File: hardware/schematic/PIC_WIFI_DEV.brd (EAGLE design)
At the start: 111.5 x 26.4 mm, 60 parts, among them J5 POWER_JACKPTH, Q1 8MHz, Q2 32.768KHz, U1 PIC32MX460F512L TQFP100, U4 RECOM_X.X_REG78XX

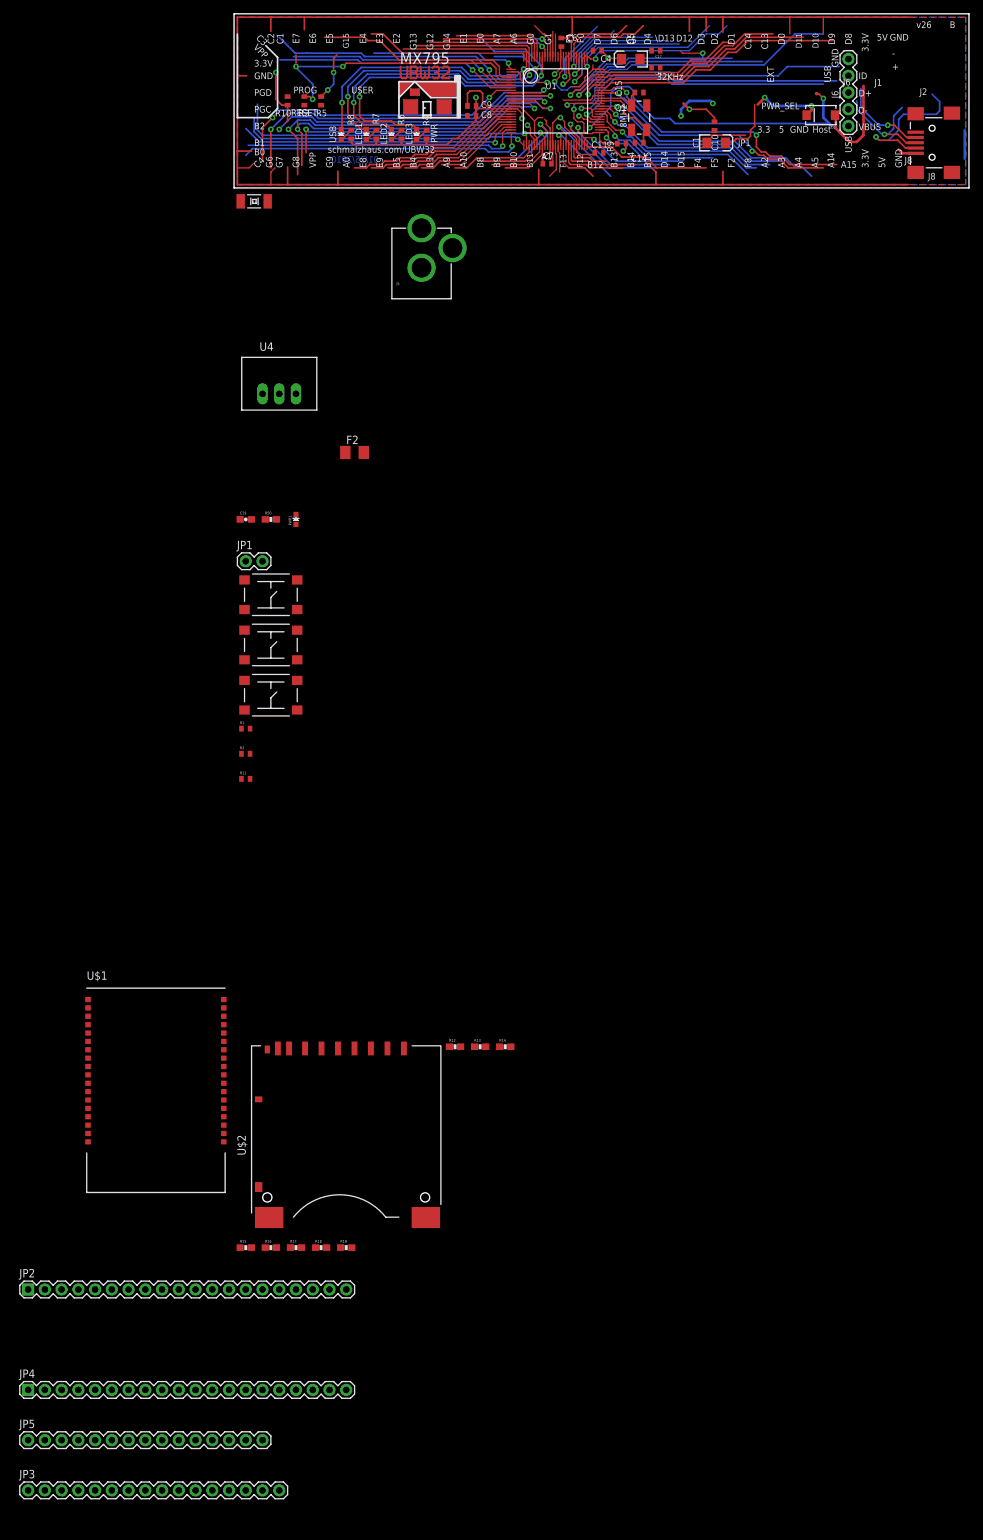
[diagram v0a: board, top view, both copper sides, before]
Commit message: Added fuse holder to lib.  Swapped 10k res for 2 4.7K in dev board.  Added fuse to waterworx.sch
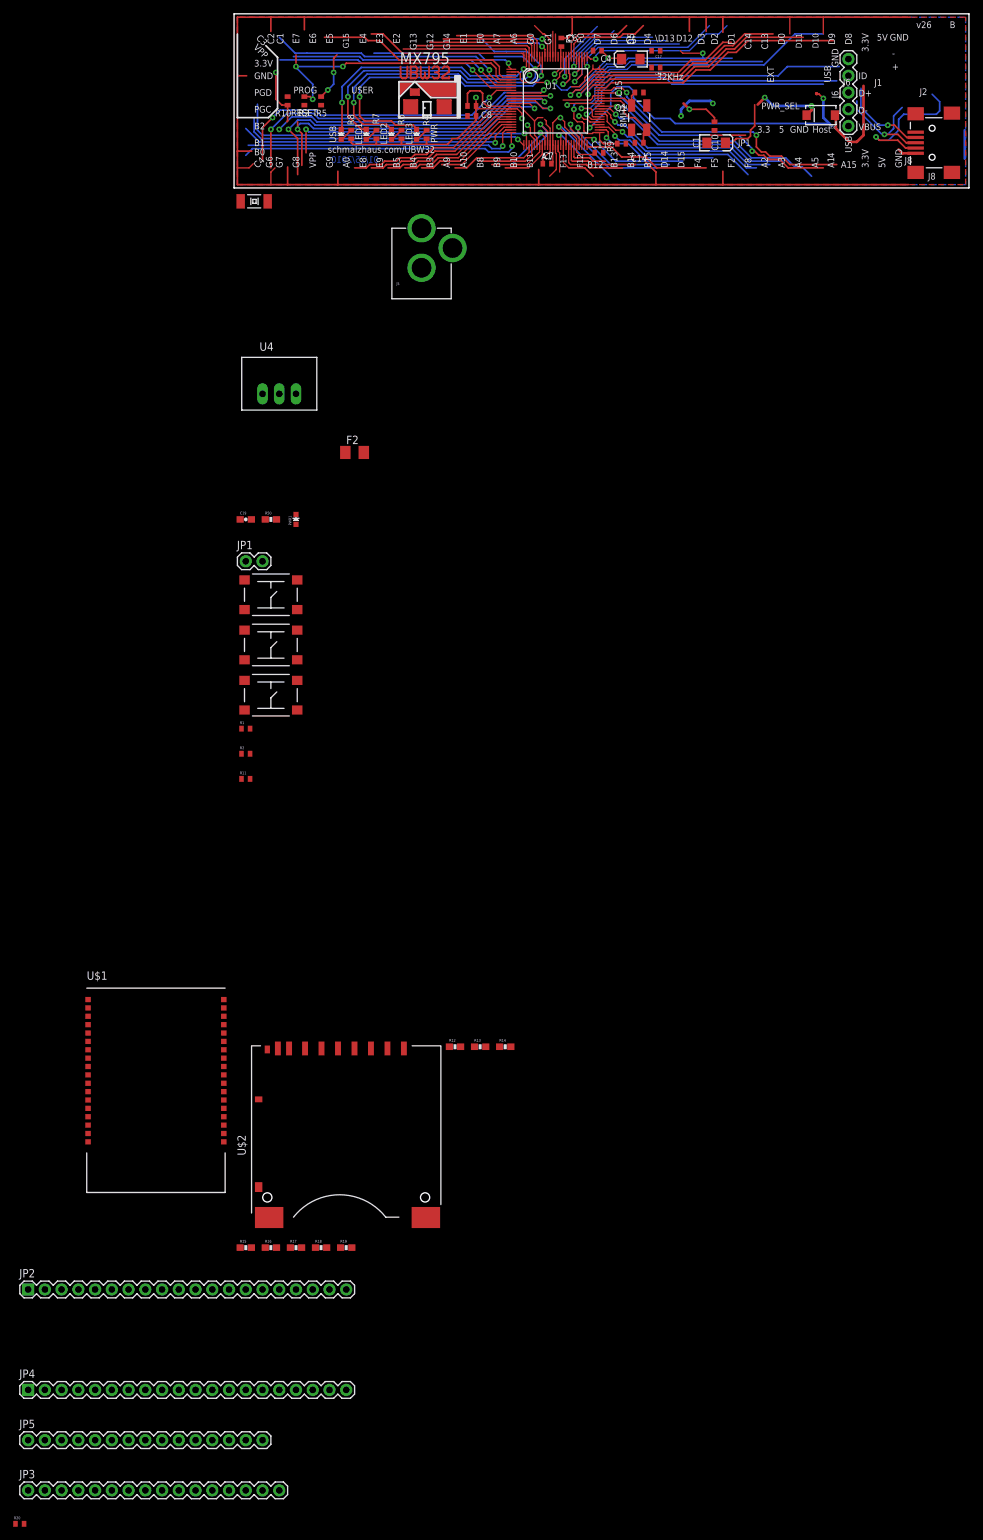
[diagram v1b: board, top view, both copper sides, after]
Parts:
- added R20: 4.7K, SparkFun:C0402
- R9: value 10K -> 4.7K
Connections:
- new net N$6: R20.1, R9.2
- net 3.3V: now also R20.2; no longer R9.2
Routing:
- net 3.3V: track 87.3 -> 86.0 mm, vias 10 -> 9
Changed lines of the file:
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@@
 <layer number="37" name="tTest" color="7" fill="1" visible="no" active="yes"/>
 <layer number="38" name="bTest" color="7" fill="1" visible="no" active="yes"/>
-<layer number="39" name="tKeepout" color="4" fill="11" visible="yes" active="yes"/>
+<layer number="39" name="tKeepout" color="4" fill="11" visible="no" active="yes"/>
 <layer number="40" name="bKeepout" color="1" fill="11" visible="no" active="yes"/>
-<layer number="41" name="tRestrict" color="4" fill="10" visible="yes" active="yes"/>
+<layer number="41" name="tRestrict" color="4" fill="10" visible="no" active="yes"/>
 <layer number="42" name="bRestrict" color="1" fill="10" visible="no" active="yes"/>
 <layer number="43" name="vRestrict" color="2" fill="10" visible="no" active="yes"/>
@@
 <layer number="121" name="_tsilk" color="14" fill="1" visible="no" active="yes"/>
 <layer number="122" name="_bsilk" color="14" fill="1" visible="no" active="yes"/>
-<layer number="125" name="_tNames" color="7" fill="1" visible="yes" active="yes"/>
-<layer number="144" name="Drill_legend" color="7" fill="1" visible="yes" active="yes"/>
+<layer number="125" name="_tNames" color="7" fill="1" visible="no" active="yes"/>
+<layer number="144" name="Drill_legend" color="7" fill="1" visible="no" active="yes"/>
 <layer number="151" name="HeatSink" color="7" fill="1" visible="no" active="no"/>
 <layer number="200" name="200bmp" color="1" fill="10" visible="no" active="no"/>
@@
 <layer number="207" name="207bmp" color="8" fill="10" visible="no" active="yes"/>
 <layer number="208" name="208bmp" color="9" fill="10" visible="no" active="yes"/>
-<layer number="209" name="209bmp" color="7" fill="1" visible="yes" active="yes"/>
-<layer number="210" name="210bmp" color="7" fill="1" visible="yes" active="yes"/>
-<layer number="211" name="211bmp" color="7" fill="1" visible="yes" active="yes"/>
-<layer number="212" name="212bmp" color="7" fill="1" visible="yes" active="yes"/>
-<layer number="213" name="213bmp" color="7" fill="1" visible="yes" active="yes"/>
-<layer number="214" name="214bmp" color="7" fill="1" visible="yes" active="yes"/>
-<layer number="215" name="215bmp" color="7" fill="1" visible="yes" active="yes"/>
-<layer number="216" name="216bmp" color="7" fill="1" visible="yes" active="yes"/>
+<layer number="209" name="209bmp" color="7" fill="1" visible="no" active="yes"/>
+<layer number="210" name="210bmp" color="7" fill="1" visible="no" active="yes"/>
+<layer number="211" name="211bmp" color="7" fill="1" visible="no" active="yes"/>
+<layer number="212" name="212bmp" color="7" fill="1" visible="no" active="yes"/>
+<layer number="213" name="213bmp" color="7" fill="1" visible="no" active="yes"/>
+<layer number="214" name="214bmp" color="7" fill="1" visible="no" active="yes"/>
+<layer number="215" name="215bmp" color="7" fill="1" visible="no" active="yes"/>
+<layer number="216" name="216bmp" color="7" fill="1" visible="no" active="yes"/>
 <layer number="217" name="217bmp" color="18" fill="1" visible="no" active="no"/>
 <layer number="218" name="218bmp" color="19" fill="1" visible="no" active="no"/>
@@
 <attribute name="VALUE" x="16.129" y="9.017" size="1.016" layer="27" rot="R90"/>
 </element>
-<element name="R9" library="SparkFun" package="C0402" value="10K" x="58.293" y="6.223" smashed="yes">
+<element name="R9" library="SparkFun" package="C0402" value="4.7K" x="58.293" y="6.223" smashed="yes">
 <attribute name="NAME" x="57.0865" y="4.953" size="1.016" layer="25" rot="R90"/>
 <attribute name="VALUE" x="58.801" y="7.874" size="1.016" layer="27" rot="R180"/>
@@
 <element name="JP5" library="SparkFun-Connectors" package="1X15" value="M15" x="-31.75" y="-190.5"/>
 <element name="JP3" library="SparkFun-Connectors" package="1X16" value="M16PTH" x="-31.75" y="-198.12"/>
+<element name="R20" library="SparkFun" package="C0402" value="4.7K" x="-33.02" y="-203.2"/>
 </elements>
 <signals>
@@
 <contactref element="U1" pad="62"/>
 <contactref element="U1" pad="55"/>
-<contactref element="R9" pad="2"/>
 <wire x1="49.06" y1="17.691" x2="49.06" y2="19.4" width="0.2032" layer="1"/>
 <wire x1="48.133" y1="16.764" x2="49.06" y2="17.691" width="0.2032" layer="1"/>
@@
 <wire x1="110.363" y1="3.937" x2="110.363" y2="8.255" width="0.4064" layer="16"/>
 <wire x1="67.691" y1="12.319" x2="68.58" y2="11.43" width="0.4064" layer="1"/>
-<wire x1="58.943" y1="6.223" x2="58.943" y2="5.476" width="0.254" layer="1"/>
-<wire x1="58.943" y1="5.476" x2="58.547" y2="5.08" width="0.254" layer="1"/>
 <wire x1="49.06" y1="19.4" x2="49.06" y2="20.851" width="0.2032" layer="1"/>
 <wire x1="49.06" y1="20.851" x2="49.149" y2="20.94" width="0.2032" layer="1" curve="-90"/>
@@
 <via x="50.038" y="12.065" extent="1-16" drill="0.381"/>
 <via x="68.58" y="11.43" extent="1-16" drill="0.381"/>
-<via x="58.547" y="5.08" extent="1-16" drill="0.381"/>
 <polygon width="0.254" layer="16" isolate="0.254">
 <vertex x="0" y="0"/>
@@
 <contactref element="JP5" pad="14"/>
 <contactref element="JP3" pad="2"/>
+<contactref element="R20" pad="2"/>
+<wire x1="-29.21" y1="-198.12" x2="-32.37" y2="-203.2" width="0" layer="19" extent="1-1"/>
 <wire x1="1.27" y1="-190.5" x2="-29.21" y2="-198.12" width="0" layer="19" extent="1-1"/>
 <wire x1="0.42" y1="-161.29" x2="1.27" y2="-190.5" width="0" layer="19" extent="1-1"/>
@@
 <wire x1="43.434" y1="15.494" x2="42.475" y2="11.5" width="0" layer="19" extent="1-1"/>
 <wire x1="48.133" y1="16.764" x2="46.99" y2="15.494" width="0" layer="19" extent="1-1"/>
-<wire x1="58.547" y1="5.08" x2="54.229" y2="4.826" width="0" layer="19" extent="1-1"/>
-<wire x1="67.691" y1="12.319" x2="58.943" y2="6.223" width="0" layer="19" extent="1-1"/>
+<wire x1="67.691" y1="12.319" x2="54.96" y2="12.3" width="0" layer="19" extent="1-1"/>
 <wire x1="92.71" y1="11.43" x2="72.39" y2="10.16" width="0" layer="19" extent="1-1"/>
 <wire x1="110.363" y1="8.255" x2="92.71" y2="11.43" width="0" layer="19" extent="16-16"/>
@@
 <wire x1="41.56" y1="16.7" x2="3.81" y2="-167.64" width="0" layer="19" extent="1-1"/>
 </signal>
+<signal name="N$6">
+<contactref element="R9" pad="2"/>
+<contactref element="R20" pad="1"/>
+<wire x1="58.943" y1="6.223" x2="-33.67" y2="-203.2" width="0" layer="19" extent="1-1"/>
+</signal>
 </signals>
